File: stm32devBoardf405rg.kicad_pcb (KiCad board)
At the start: 4 copper layers, 54 parts, among them J1 Screw_Terminal_01x02, J2 SWD, J3 Conn_01x04, J4 Conn_01x04, J5 USB_B_Micro, Q1 AO3401A, SW1 SW_SPDT, U1 STM32F405RGT6, U2 USBLC6-2SC6, Y1 16MZ

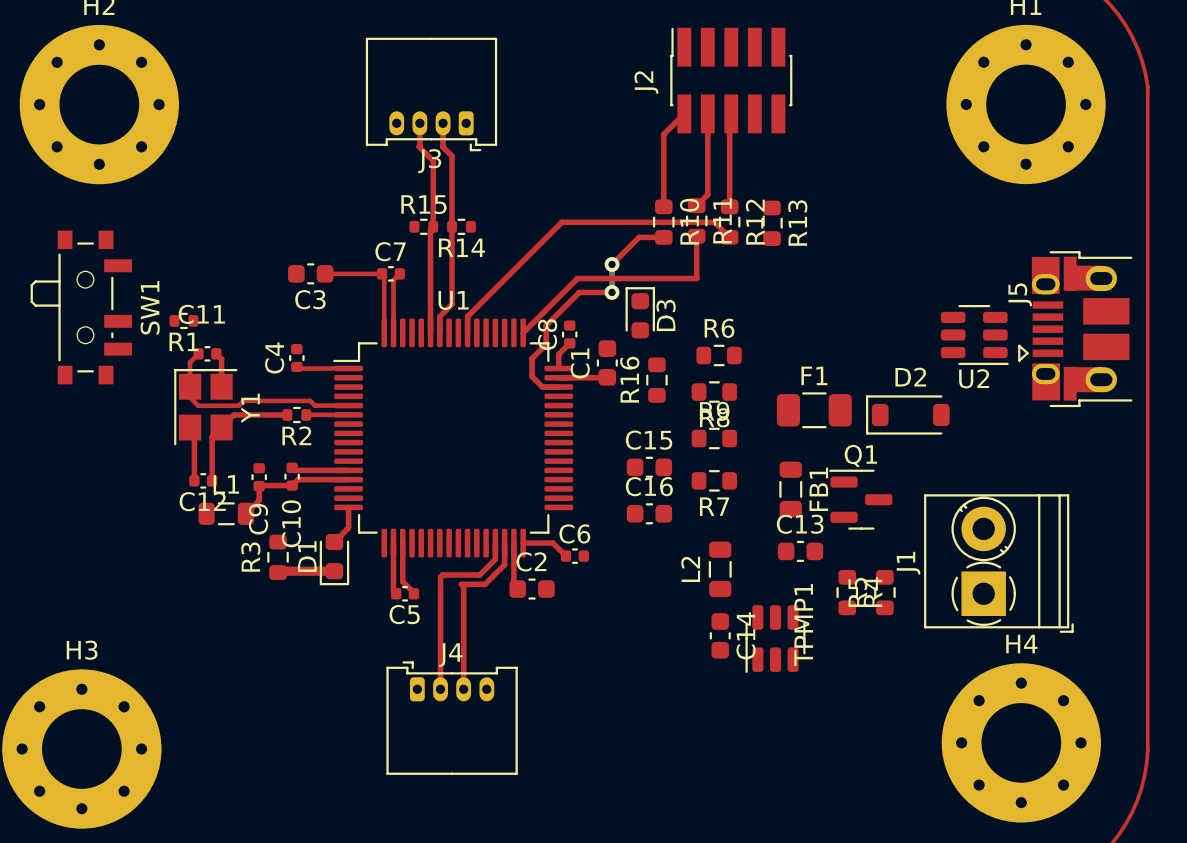
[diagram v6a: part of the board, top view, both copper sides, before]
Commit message: added more routes
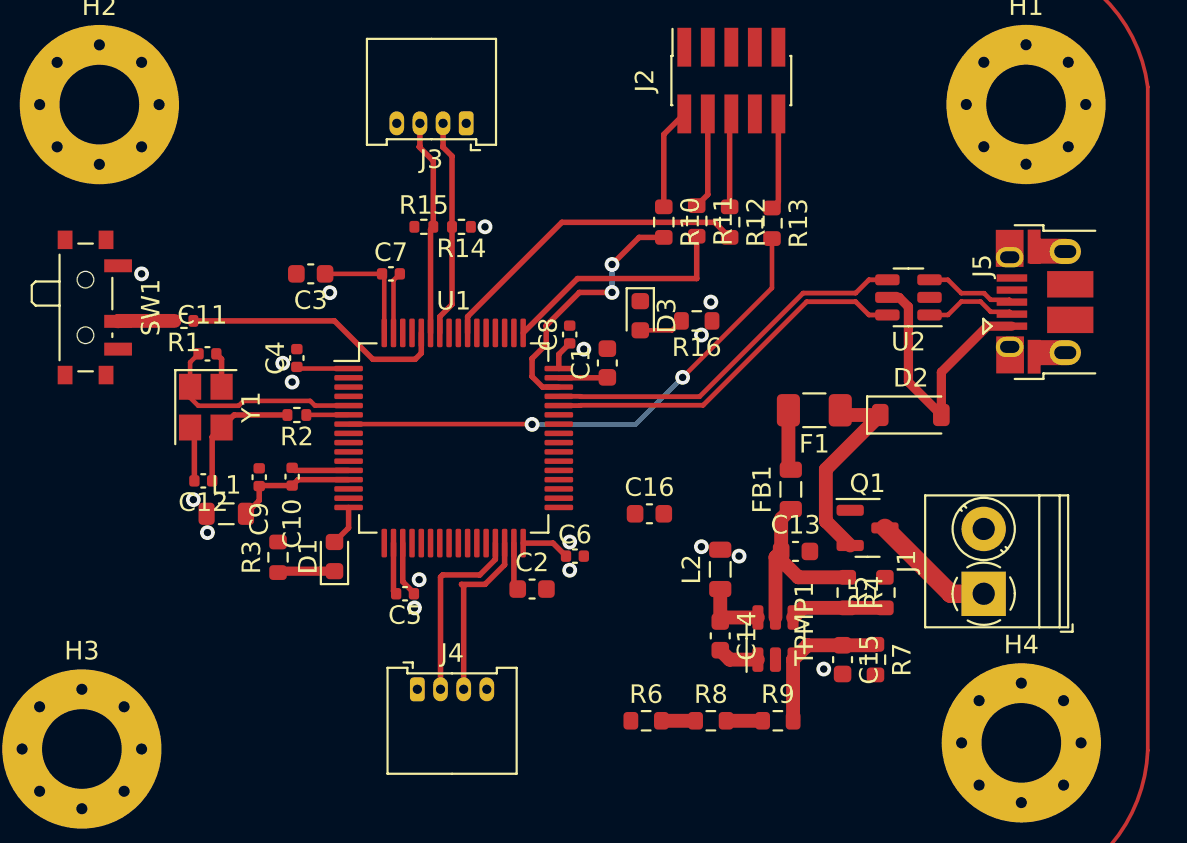
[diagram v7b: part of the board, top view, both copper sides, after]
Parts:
- moved R6 20.1 mm to (106.2, 149.1)
- moved R8 17.8 mm to (109.7, 149.1), turned to 0 degrees
- moved R9 15.6 mm to (113.3, 149.1)
- moved C15 14.7 mm to (116.8, 145.8), turned to -90 degrees
- moved R7 13.0 mm to (118.6, 145.8), turned to -90 degrees
- moved U2 4.10 mm to (120.4, 126.2)
- moved R16 3.85 mm to (109.0, 127.5), turned to 180 degrees
- moved J5 2.43 mm to (127.7, 126.5)
- moved Q1 1.56 mm to (118.2, 138.7)
- moved C13 0.27 mm to (114.3, 140.0)
- turned F1 to 180 degrees
- turned FB1 to 90 degrees
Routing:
- net NRST: track 0.00 -> 28.6 mm, vias 0 -> 2
- net USB_D-: track 0.00 -> 20.4 mm
- net USB_D+: track 0.00 -> 20.4 mm
- net +5V: track 0.00 -> 15.1 mm
- net BOOT0: track 0.00 -> 14.4 mm
- net Net-(D2-K): track 0.00 -> 11.1 mm
- net BUCK_IN: track 0.00 -> 10.6 mm
- net BUCK_FB: track 0.00 -> 8.10 mm
- net +12V: track 0.00 -> 6.81 mm
- net Net-(J2-Pin_10): track 0.00 -> 5.22 mm
- net BUCK_EN: track 0.00 -> 5.17 mm
- net USB_CONN_D-: track 0.00 -> 5.03 mm
- net USB_CONN_D+: track 0.00 -> 4.95 mm
- net BUCK_SW: track 0.00 -> 3.87 mm
- net Net-(F1-Pad2): track 0.00 -> 3.26 mm
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
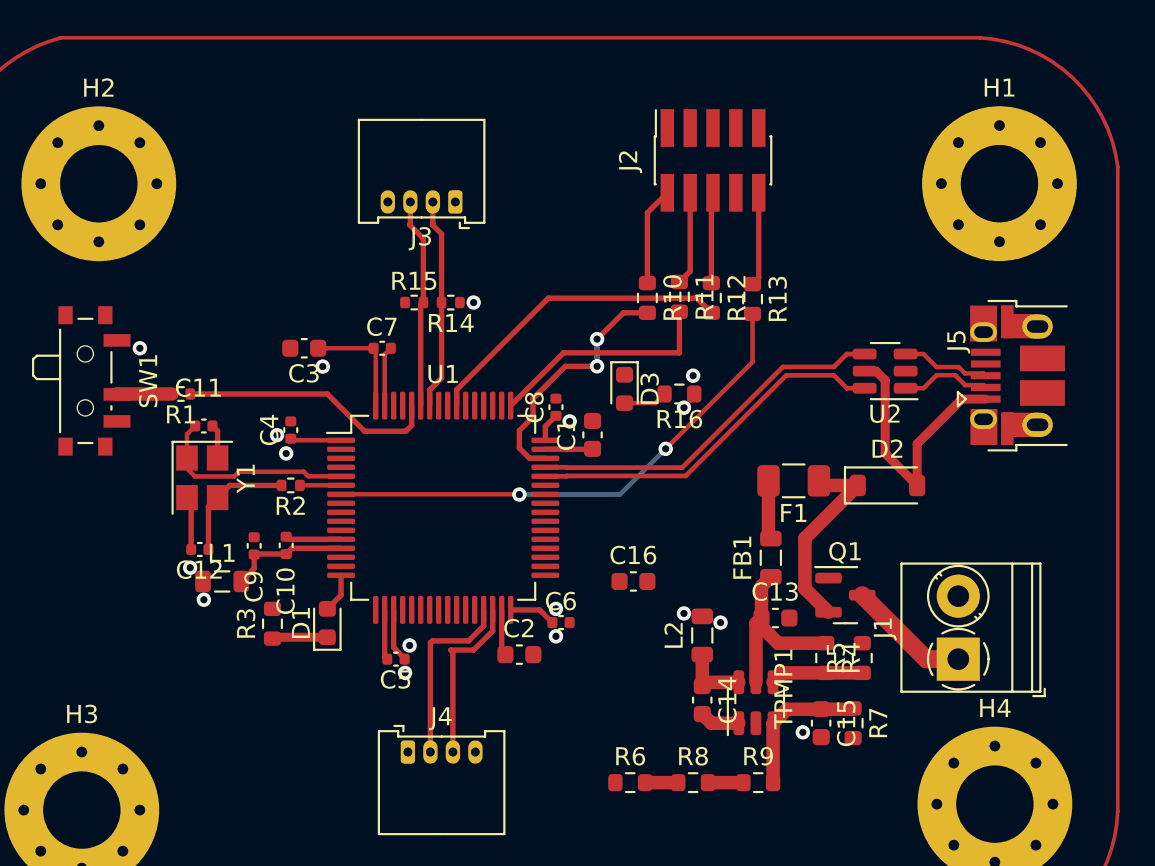
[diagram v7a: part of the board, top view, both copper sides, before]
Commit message: added 3.3v and grd vias
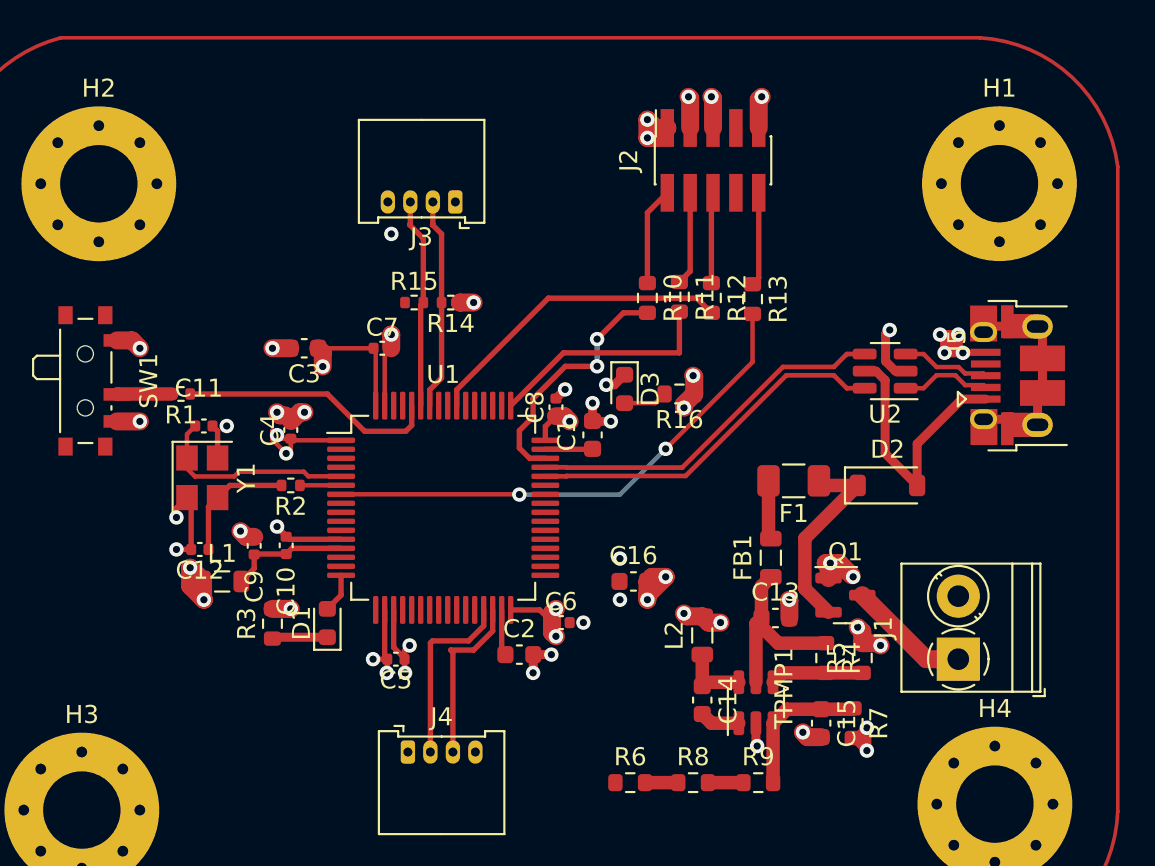
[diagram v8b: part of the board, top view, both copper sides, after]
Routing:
- net GND: track 14.1 -> 58.1 mm, vias 0 -> 39
- net +3.3V: track 16.3 -> 44.7 mm, vias 17 -> 21
- net unconnected-(J5-Shield-Pad6): track 0.00 -> 10.9 mm
